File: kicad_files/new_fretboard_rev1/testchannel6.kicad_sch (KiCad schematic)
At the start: 22 parts, among them U2 LX3302AQPW-TR-EASY

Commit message: all circuit traces
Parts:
- removed C12, C13: 680pf, Capacitor_SMD:C_0603_1608Metric, symbol Device:C
- removed C14, C15: 10pf, Capacitor_SMD:C_0402_1005Metric, symbol Device:C
- removed C16: 1uf, Capacitor_SMD:C_0603_1608Metric, symbol Device:C
- removed C17, C20: 100nf, Capacitor_SMD:C_0402_1005Metric, symbol Device:C
- removed C18, C19: 6.8nf, Capacitor_SMD:C_0402_1005Metric, symbol Device:C
- removed C21: 1000pf, Capacitor_SMD:C_0402_1005Metric, symbol Device:C
- removed C22: 470nf, Capacitor_SMD:C_0402_1005Metric, symbol Device:C
- removed L5, L6, L7, L8: L, NetTie:NetTie-2_SMD_Pad0.5mm, symbol Device:L
- removed R10, R11, R8, R9: 10R, Resistor_SMD:R_0402_1005Metric, symbol Device:R
- removed R12: 221R, Resistor_SMD:R_0402_1005Metric, symbol Device:R
- removed R13: 4.7R, Resistor_SMD:R_0402_1005Metric, symbol Device:R
- removed U2: LX3302AQPW-TR-EASY, Snapeda:14-TSSOP_MCH-L, symbol Snapeda:LX3302AQPW-TR-EASY
- added C67, C73: 100nf, Capacitor_SMD:C_0402_1005Metric, symbol Device:C
- added C68: 1000pf, Capacitor_SMD:C_0402_1005Metric, symbol Device:C
- added C69: 470nf, Capacitor_SMD:C_0402_1005Metric, symbol Device:C
- added C70: 1uf, Capacitor_SMD:C_0603_1608Metric, symbol Device:C
- added C71, C72: 6.8nf, Capacitor_SMD:C_0402_1005Metric, symbol Device:C
- added C74, C75: 10pf, Capacitor_SMD:C_0402_1005Metric, symbol Device:C
- added C76, C77: 680pf, Capacitor_SMD:C_0603_1608Metric, symbol Device:C
- added L25, L26, L27, L28: L, NetTie:NetTie-2_SMD_Pad0.5mm, symbol Device:L
- added R37: 4.7R, Resistor_SMD:R_0402_1005Metric, symbol Device:R
- added R38: 221R, Resistor_SMD:R_0402_1005Metric, symbol Device:R
- added R39, R40, R41, R42: 10R, Resistor_SMD:R_0402_1005Metric, symbol Device:R
- added U7: LX3302AQPW-TR-EASY, Snapeda:14-TSSOP_MCH-L, symbol Snapeda:LX3302AQPW-TR-EASY
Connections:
- net CL1B_A: now also L28.1, R42.2
- net CL1_A: now also C74.1, R42.1, U7.8 (CL1)
- net CL2B_A: now also L27.1, R41.2
- net CL2_A: now also C75.1, R41.1, U7.10 (CL2)
- net GND: now also C67.1, C68.1, C69.1, C70.1, C71.1, C72.1, C74.2, C75.2, C76.2, C77.2, L27.2, L28.2, U7.2 (GND), U7.9 (GNDCL)
- net OSC11_A: now also C76.1, L25.2, U7.13 (OSC1)
- net OSC12_A: now also C77.1, L26.2, U7.12 (OSC2)
- net SUB_A: now also C73.1, U7.11 (SUB)
- net VIN_A: now also C68.2, C69.2, R37.1, R39.2, R40.1, U7.4 (VIN)
- new net: C70.2, C73.2, U7.5 (VDD)
- new net: C67.2, R37.2
- new net: C71.2, R38.2
- new net: C72.2, R38.1, R39.1, U7.6 (IO2)
- new net /OSC2B_A: L25.1, L26.1, R40.2
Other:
- removed sheet testchannel1
- removed sheet testchannel2
- removed sheet testchannel3
- removed sheet testchannel4
- removed sheet testchannel5
- removed sheet testchannel6
- removed sheet testchannel7

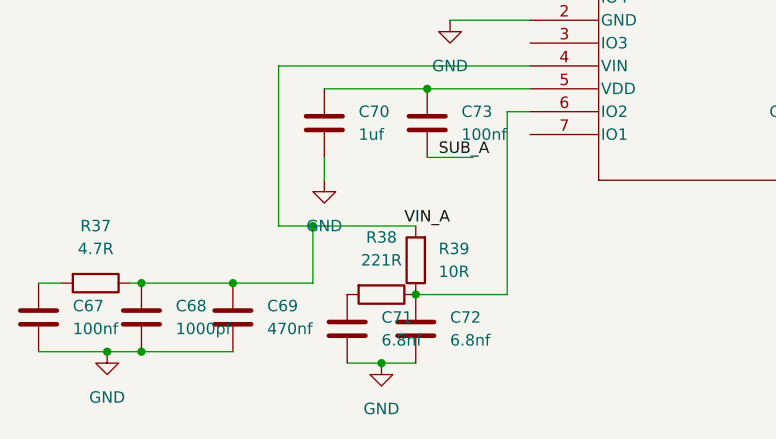
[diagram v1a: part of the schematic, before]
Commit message: stm32 micro added
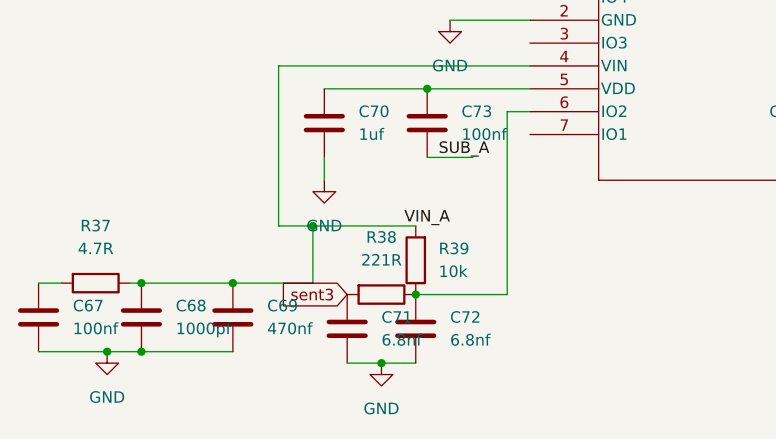
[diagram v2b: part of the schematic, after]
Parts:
- R39: value 10R -> 10k
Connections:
- net sent3: now reaches C71.2, R38.2
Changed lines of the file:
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@@
+		)
+	)
+	(global_label "sent3"
+		(shape input)
+		(at 88.9 125.73 180)
+		(fields_autoplaced yes)
+		(effects
+			(font
+				(size 1.27 1.27)
+			)
+			(justify right)
+		)
+		(property "Intersheetrefs" "${INTERSHEET_REFS}"
+			(at 80.7139 125.73 0)
+			(effects
+				(font
+					(size 1.27 1.27)
+				)
+				(justify right)
+				(hide yes)
+			)
 		)
 	)
@@
 			)
 		)
-		(property "Component Class" ""
-			(at 97.79 106.68 0)
-			(effects
-				(font
-					(size 1.27 1.27)
-				)
-				(hide yes)
-			)
-		)
 		(pin "1"
 		)
@@
 			)
 		)
-		(property "Component Class" ""
-			(at 162.56 57.15 0)
-			(effects
-				(font
-					(size 1.27 1.27)
-				)
-				(hide yes)
-			)
-		)
 		(pin "2"
 		)
@@
 			)
 		)
-		(property "Component Class" ""
-			(at 181.61 121.92 90)
-			(effects
-				(font
-					(size 1.27 1.27)
-				)
-				(hide yes)
-			)
-		)
 		(pin "1"
 		)
@@
 			)
 		)
-		(property "Component Class" ""
-			(at 60.96 124.46 90)
-			(effects
-				(font
-					(size 1.27 1.27)
-				)
-				(hide yes)
-			)
-		)
 		(pin "2"
 		)
@@
 			)
 		)
-		(property "Component Class" ""
-			(at 88.9 129.54 0)
-			(effects
-				(font
-					(size 1.27 1.27)
-				)
-				(hide yes)
-			)
-		)
 		(pin "1"
 		)
@@
 			)
 		)
-		(property "Component Class" ""
-			(at 92.71 125.73 90)
-			(effects
-				(font
-					(size 1.27 1.27)
-				)
-				(hide yes)
-			)
-		)
 		(pin "2"
 		)
@@
 			)
 		)
-		(property "Component Class" ""
-			(at 76.2 128.27 0)
-			(effects
-				(font
-					(size 1.27 1.27)
-				)
-				(hide yes)
-			)
-		)
 		(pin "1"
 		)
@@
 			)
 		)
-		(property "Component Class" ""
-			(at 54.61 128.27 0)
-			(effects
-				(font
-					(size 1.27 1.27)
-				)
-				(hide yes)
-			)
-		)
 		(pin "1"
 		)
@@
 			)
 		)
-		(property "Component Class" ""
-			(at 168.91 102.87 90)
-			(effects
-				(font
-					(size 1.27 1.27)
-				)
-				(hide yes)
-			)
-		)
 		(pin "1"
 		)
@@
 			)
 		)
-		(property "Component Class" ""
-			(at 162.56 68.58 0)
-			(effects
-				(font
-					(size 1.27 1.27)
-				)
-				(hide yes)
-			)
-		)
 		(pin "1"
 		)
@@
 			)
 		)
-		(property "Component Class" ""
-			(at 96.52 129.54 0)
-			(effects
-				(font
-					(size 1.27 1.27)
-				)
-				(hide yes)
-			)
-		)
 		(pin "1"
 		)
@@
 			)
 		)
-		(property "Component Class" ""
-			(at 181.61 113.03 90)
-			(effects
-				(font
-					(size 1.27 1.27)
-				)
-				(hide yes)
-			)
-		)
 		(pin "1"
 		)
@@
 			)
 		)
-		(property "Component Class" ""
-			(at 167.64 133.35 90)
-			(effects
-				(font
-					(size 1.27 1.27)
-				)
-				(hide yes)
-			)
-		)
 		(pin "1"
 		)
@@
 			)
 		)
-		(property "Component Class" ""
-			(at 170.18 121.92 90)
-			(effects
-				(font
-					(size 1.27 1.27)
-				)
-				(hide yes)
-			)
-		)
 		(pin "2"
 		)
@@
 			)
 		)
-		(property "Component Class" ""
-			(at 182.88 85.09 90)
-			(effects
-				(font
-					(size 1.27 1.27)
-				)
-				(hide yes)
-			)
-		)
 		(pin "1"
 		)
@@
 			)
 		)
-		(property "Value" "10R"
+		(property "Value" "10k"
 			(at 99.06 123.1899 0)
 			(effects
@@
 			)
 		)
-		(property "Component Class" ""
-			(at 96.52 121.92 0)
-			(effects
-				(font
-					(size 1.27 1.27)
-				)
-				(hide yes)
-			)
-		)
 		(pin "2"
 		)
@@
 			)
 		)
-		(property "Component Class" ""
-			(at 168.91 113.03 90)
-			(effects
-				(font
-					(size 1.27 1.27)
-				)
-				(hide yes)
-			)
-		)
 		(pin "2"
 		)
@@
 			)
 		)
-		(property "Component Class" ""
-			(at 109.22 92.71 0)
-			(effects
-				(font
-					(size 1.27 1.27)
-				)
-				(hide yes)
-			)
-		)
 		(pin "5"
 		)
@@
 			)
 		)
-		(property "Component Class" ""
-			(at 182.88 97.79 90)
-			(effects
-				(font
-					(size 1.27 1.27)
-				)
-				(hide yes)
-			)
-		)
 		(pin "1"
 		)
@@
 			)
 		)
-		(property "Component Class" ""
-			(at 172.72 68.58 0)
-			(effects
-				(font
-					(size 1.27 1.27)
-				)
-				(hide yes)
-			)
-		)
 		(pin "1"
 		)
@@
 			)
 		)
-		(property "Component Class" ""
-			(at 86.36 106.68 0)
-			(effects
-				(font
-					(size 1.27 1.27)
-				)
-				(hide yes)
-			)
-		)
 		(pin "1"
 		)
@@
 			(at 66.04 128.27 0)
 			(effects
-				(font
-					(size 1.27 1.27)
-				)
-				(hide yes)
-			)
-		)
-		(property "Component Class" ""
-			(at 66.04 128.27 0)
-			(effects

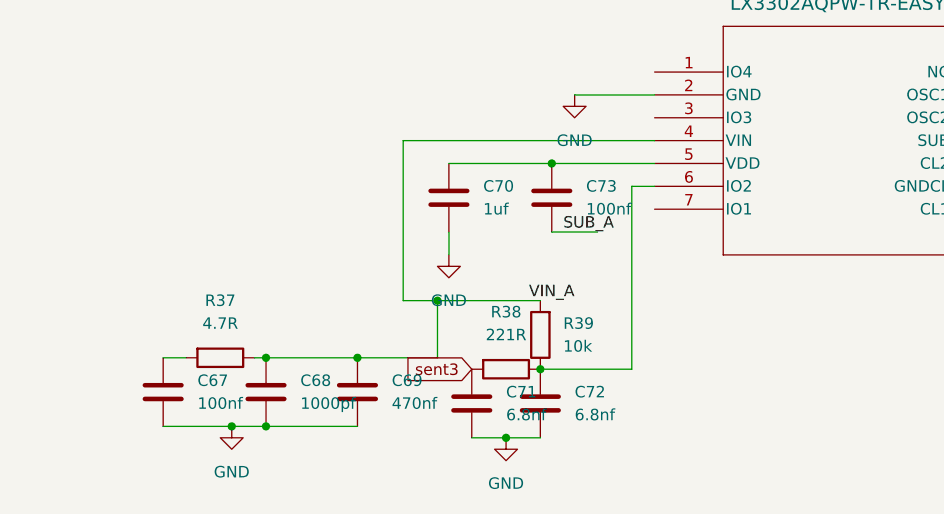
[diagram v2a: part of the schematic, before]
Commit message: mcu configured, still needs power connections and spi i2c connections
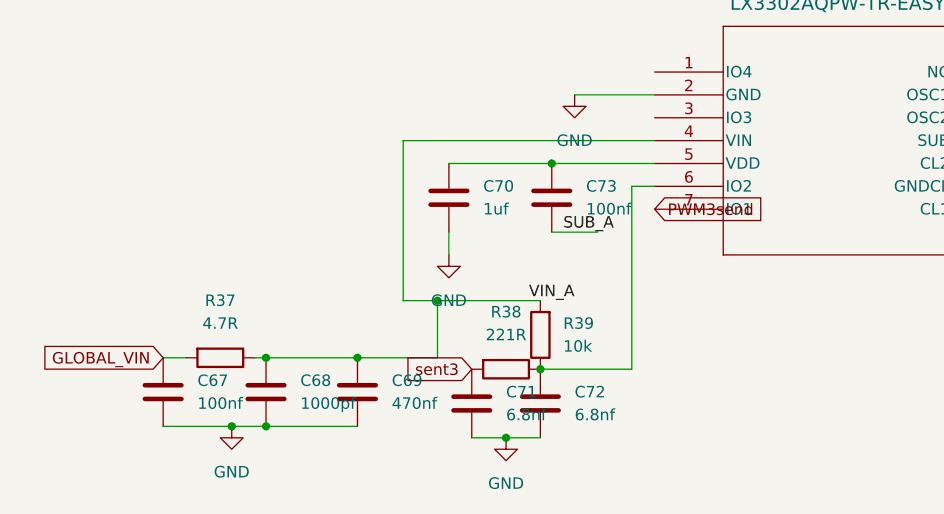
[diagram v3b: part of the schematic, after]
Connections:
- net GLOBAL_VIN: now reaches C67.2, R37.2
- net PWM3send: now reaches U7.7 (IO1)
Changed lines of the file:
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@@
+		)
+	)
+	(global_label "GLOBAL_VIN"
+		(shape input)
+		(at 54.61 124.46 180)
+		(fields_autoplaced yes)
+		(effects
+			(font
+				(size 1.27 1.27)
+			)
+			(justify right)
+		)
+		(property "Intersheetrefs" "${INTERSHEET_REFS}"
+			(at 40.618 124.46 0)
+			(effects
+				(font
+					(size 1.27 1.27)
+				)
+				(justify right)
+				(hide yes)
+			)
+		)
+	)
+	(global_label "PWM3send"
+		(shape input)
+		(at 109.22 107.95 0)
+		(fields_autoplaced yes)
+		(effects
+			(font
+				(size 1.27 1.27)
+			)
+			(justify left)
+		)
+		(property "Intersheetrefs" "${INTERSHEET_REFS}"
+			(at 122.0022 107.95 0)
+			(effects
+				(font
+					(size 1.27 1.27)
+				)
+				(justify left)
+				(hide yes)
+			)
 		)
 	)

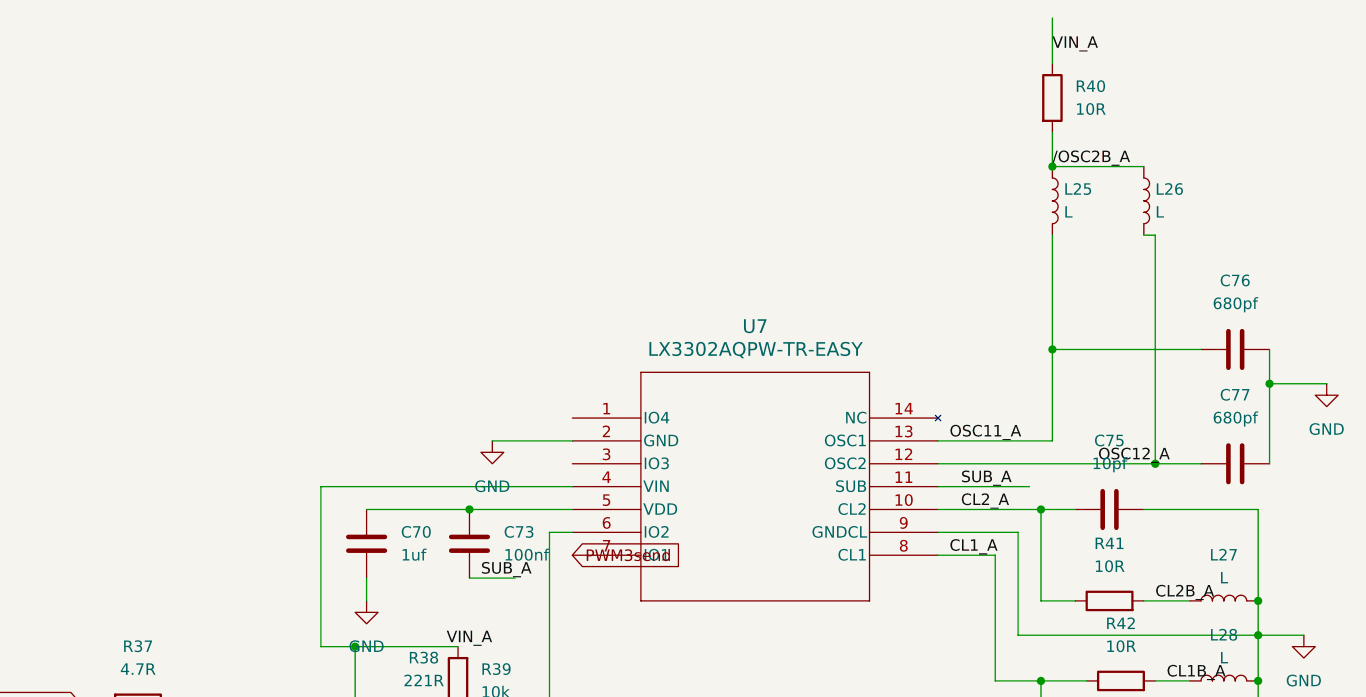
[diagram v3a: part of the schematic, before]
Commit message: finished routing - adding silkscreen
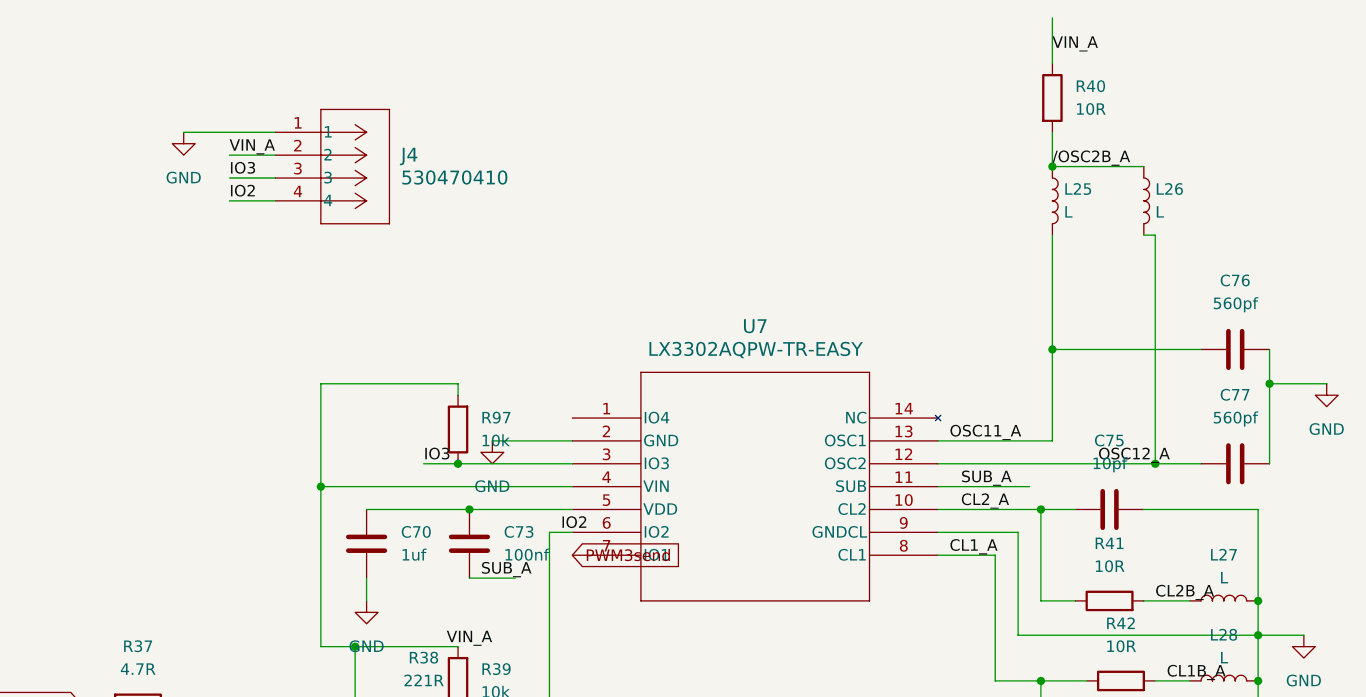
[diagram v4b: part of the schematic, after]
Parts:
- added J4: 530470410, Snapeda:CONN04_530470410_MOL, symbol Snapeda:530470410
- added R97: 10k, Resistor_SMD:R_0402_1005Metric, symbol Device:R
- C76, C77: value 680pf -> 560pf
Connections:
- net GND: now also J4.1
- net VIN_A: now also J4.2, R97.2
- net IO2: now reaches C72.2, R38.1, R39.1, U7.6 (IO2)
- net IO2: now also J4.4
- net IO3: now reaches U7.3 (IO3)
- net IO3: now also J4.3, R97.1

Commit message: exported gerbers of lefthand
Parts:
- L25, L26, L27, L28: now left out of the parts list
